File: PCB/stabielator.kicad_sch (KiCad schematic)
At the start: 28 parts, among them SW2 BOOT, U3 ESP32-C3-MINI-1

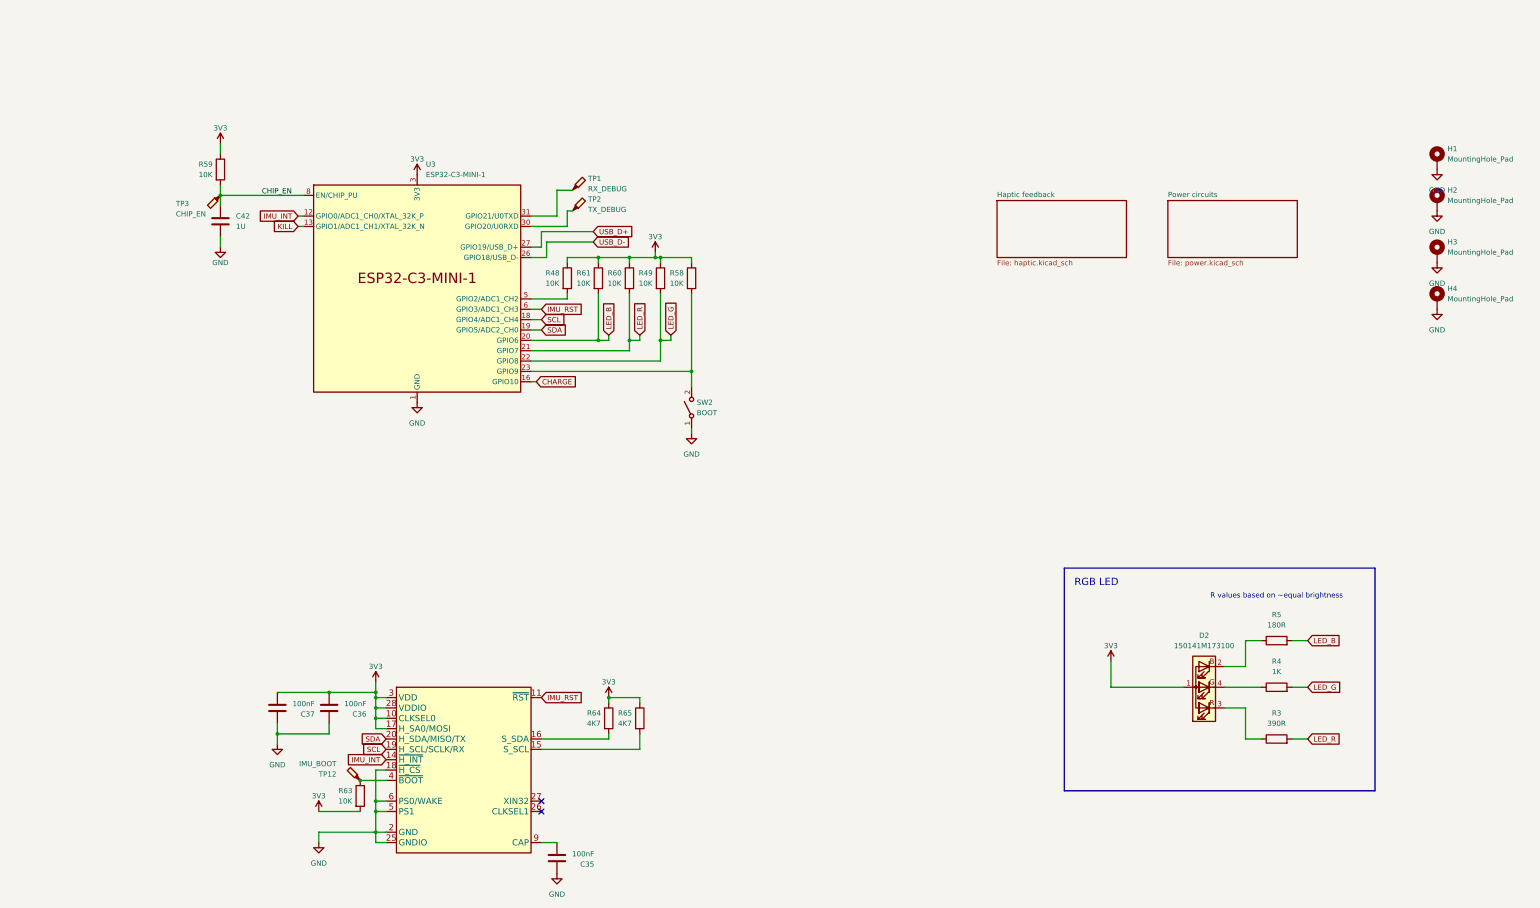
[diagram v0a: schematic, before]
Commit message: Review schematic
Fix errors / add improvements
Add gitignore file
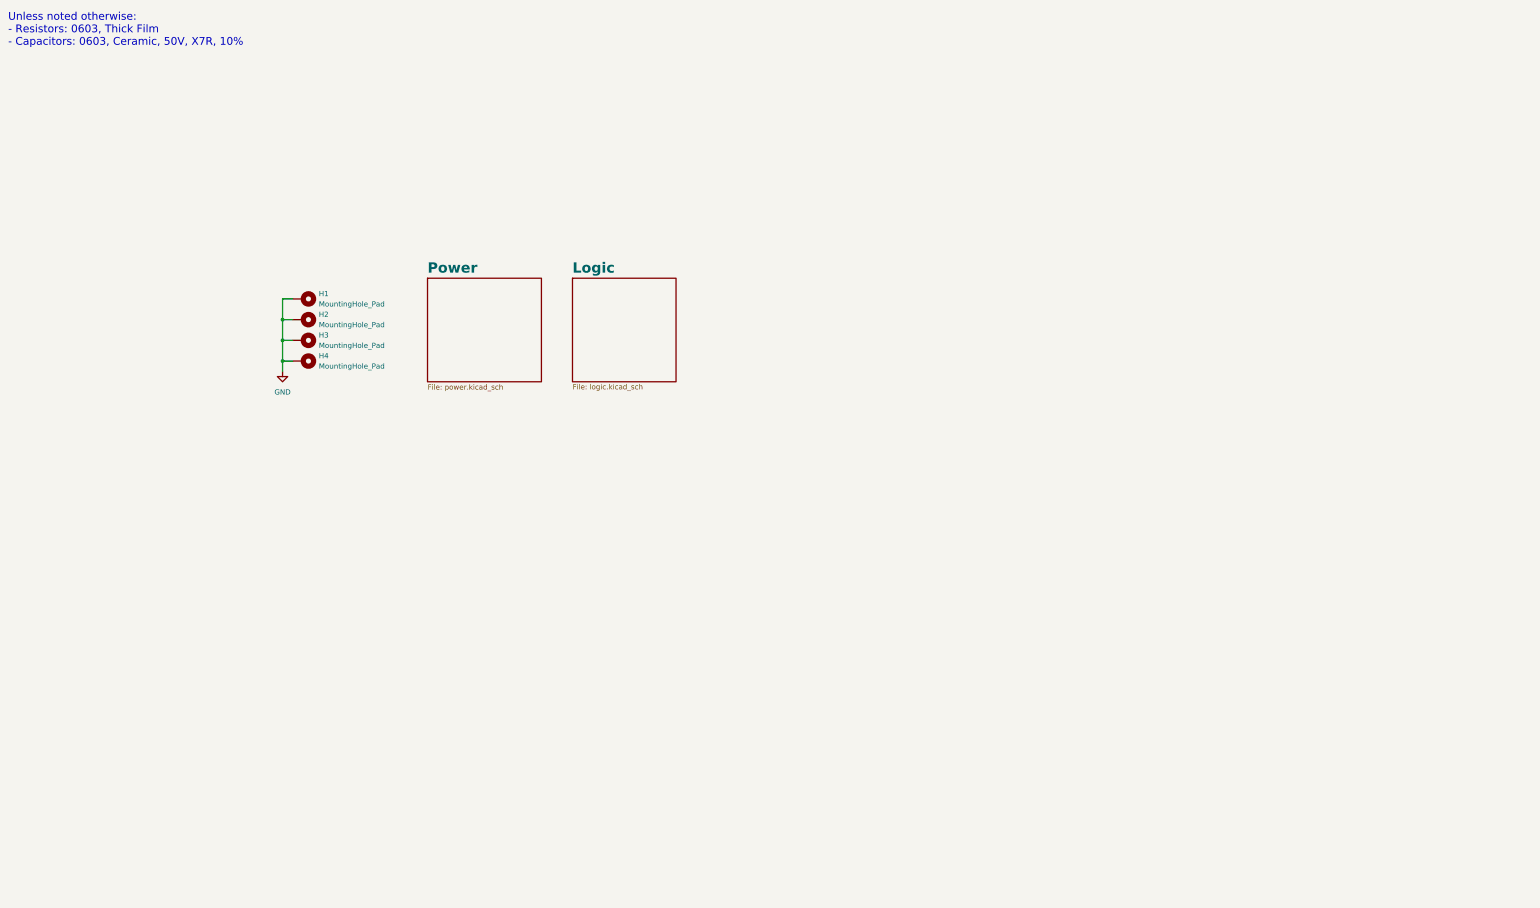
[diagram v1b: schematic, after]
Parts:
- removed C35, C36, C37: 100nF, Capacitor_SMD:C_0603_1608Metric, symbol Device:C
- removed C42: 1U, Capacitor_SMD:C_0603_1608Metric, symbol Device:C
- removed D2: 150141M173100, LED_SMD:LED_RGB_Wuerth-PLCC4_3.2x2.8mm_150141M173100, symbol Device:LED_ABRG
- removed R3: 390R, Resistor_SMD:R_0603_1608Metric, symbol Device:R
- removed R4: 1K, Resistor_SMD:R_0603_1608Metric, symbol Device:R
- removed R48, R49, R58, R59, R60, R61, R63: 10K, Resistor_SMD:R_0603_1608Metric, symbol Device:R
- removed R5: 180R, Resistor_SMD:R_0603_1608Metric, symbol Device:R
- removed R64, R65: 4K7, Resistor_SMD:R_0603_1608Metric, symbol Device:R
- removed SW2: BOOT, Button_Switch_SMD:SW_SPST_B3U-1000P, symbol Switch:SW_SPST
- removed TP1: RX_DEBUG, TestPoint:TestPoint_Pad_D1.0mm, symbol Connector:TestPoint_Probe
- removed TP12: IMU_BOOT, TestPoint:TestPoint_Pad_D1.0mm, symbol Connector:TestPoint_Probe
- removed TP2: TX_DEBUG, TestPoint:TestPoint_Pad_D1.0mm, symbol Connector:TestPoint_Probe
- removed TP3: CHIP_EN, TestPoint:TestPoint_Pad_D1.0mm, symbol Connector:TestPoint_Probe
- removed U2: (no value), stabielator:LGA-28, symbol stabielator:BNO086
- removed U3: ESP32-C3-MINI-1, PCM_Espressif:ESP32-C3-MINI-1, symbol PCM_Espressif:ESP32-C3-MINI-1
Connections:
- no-connect marks 2 -> 0
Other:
- sheet Haptic feedback renamed Logic
- sheet Power circuits renamed Power
- sheet Logic: file haptic.kicad_sch -> logic.kicad_sch
- note added: "Unless noted otherwise: - Resistors: 0603, Thick Film - Capacitors: 0603, Ceramic, 50V, X7R, 10%"
- note removed: "R values based on ~equal brightness"
- note removed: "RGB LED"
- company: ProtoIoT -> ${Company_name}
- title: Stabielator -> ${Project_name}

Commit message: Hopelijk definitief schema
Voornamelijk voeding opnieuw gemaakt;
Vervangen voor een buck boost systeem.
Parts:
- H1, H2, H3, H4: Digikey (none) -> nvt
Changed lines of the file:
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@@
+			)
+		)
+		(property "Digikey" "nvt"
+			(at 88.9 99.06 90)
+			(hide yes)
+			(show_name no)
+			(do_not_autoplace no)
+			(effects
+				(font
+					(size 1.27 1.27)
+				)
 			)
 		)
@@
 			)
 		)
+		(property "Digikey" "nvt"
+			(at 88.9 104.14 90)
+			(hide yes)
+			(show_name no)
+			(do_not_autoplace no)
+			(effects
+				(font
+					(size 1.27 1.27)
+				)
+			)
+		)
 		(pin "1"
 		)
@@
 			)
 		)
+		(property "Digikey" "nvt"
+			(at 88.9 88.9 90)
+			(hide yes)
+			(show_name no)
+			(do_not_autoplace no)
+			(effects
+				(font
+					(size 1.27 1.27)
+				)
+			)
+		)
 		(pin "1"
 		)
@@
 			(hide yes)
 			(show_name no)
+			(do_not_autoplace no)
+			(effects
+				(font
+					(size 1.27 1.27)
+				)
+			)
+		)
+		(property "Digikey" "nvt"
+			(at 88.9 93.98 90)
+			(hide yes)
+			(show_name no)

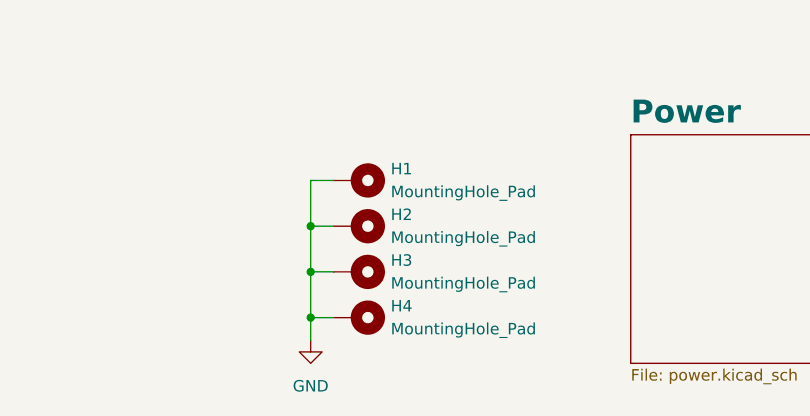
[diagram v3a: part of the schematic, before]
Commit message: Reannotated schematic based on component placement
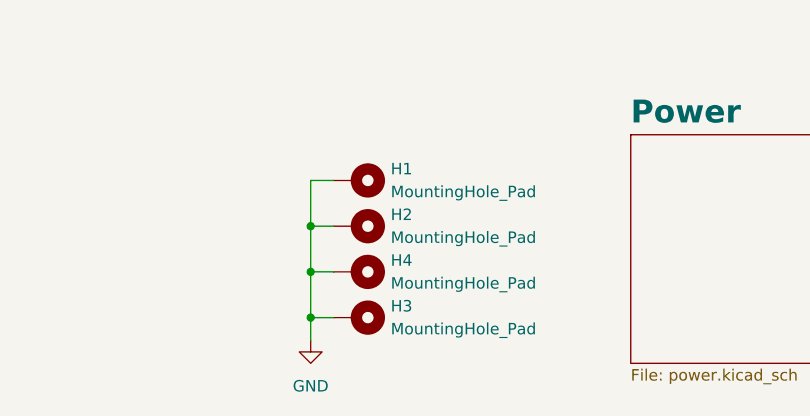
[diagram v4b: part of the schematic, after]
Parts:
- renumbered H4 to H3, H3 to H4
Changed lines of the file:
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@@
 		(dnp no)
 		(fields_autoplaced yes)
-		(property "Reference" "H3"
+		(property "Reference" "H4"
 			(at 92.71 97.7899 90)
 			(show_name no)
@@
 			(project "stabielator"
 				(path "/c0e871b7-8ed4-4f9b-ae4f-e503a34d56f3"
-					(reference "H3")
+					(reference "H4")
 					(unit 1)
 				)
@@
 		(dnp no)
 		(fields_autoplaced yes)
-		(property "Reference" "H4"
+		(property "Reference" "H3"
 			(at 92.71 102.8699 90)
 			(show_name no)
@@
 			(project "stabielator"
 				(path "/c0e871b7-8ed4-4f9b-ae4f-e503a34d56f3"
-					(reference "H4")
+					(reference "H3")
 					(unit 1)
 				)

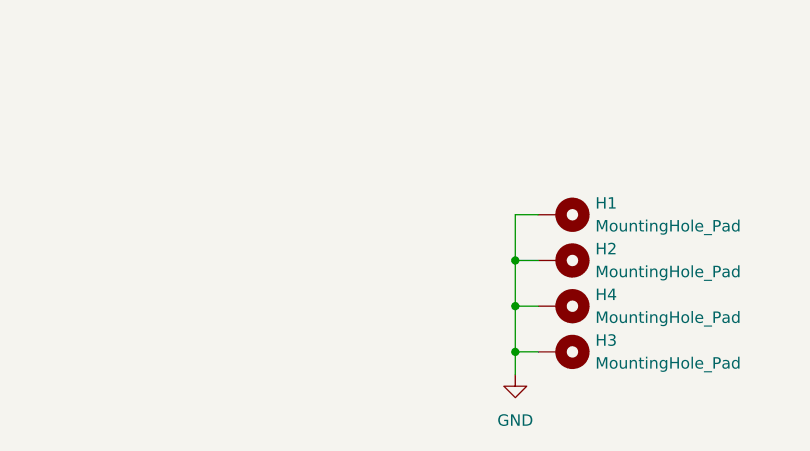
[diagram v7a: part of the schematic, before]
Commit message: Feedback Elect
- Thermal reliefs toegepast op een aantal extra onderdelen
- U7 (LGA-28) footprint pads + pasta/masker aangepast (80% pasta dekking aangeraden door fabrikant)
- Algemene soldeer masker expansie op 0 gezet
- 2x 0.5mm fiducial toegevoegd
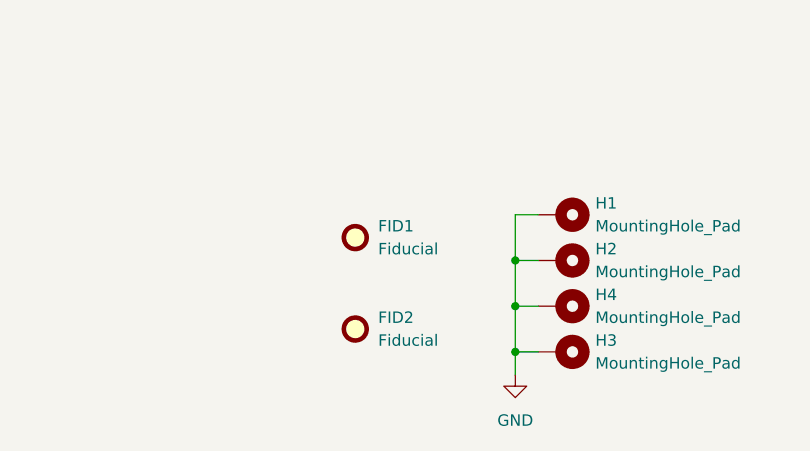
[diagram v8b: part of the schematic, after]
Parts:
- added FID1, FID2: Fiducial, Fiducial:Fiducial_0.5mm_Mask1mm, symbol symbols:Fiducial
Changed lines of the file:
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@@
+	)
+	(symbol
+		(lib_id "symbols:Fiducial")
+		(at 66.04 101.6 0)
+		(unit 1)
+		(body_style 1)
+		(exclude_from_sim no)
+		(in_bom no)
+		(on_board yes)
+		(in_pos_files yes)
+		(dnp no)
+		(fields_autoplaced yes)
+		(property "Reference" "FID2"
+			(at 68.58 100.3299 0)
+			(show_name no)
+			(do_not_autoplace no)
+			(effects
+				(font
+					(size 1.27 1.27)
+				)
+				(justify left)
+			)
+		)
+		(property "Value" "Fiducial"
+			(at 68.58 102.8699 0)
+			(show_name no)
+			(do_not_autoplace no)
+			(effects
+				(font
+					(size 1.27 1.27)
+				)
+				(justify left)
+			)
+		)
+		(property "Footprint" "Fiducial:Fiducial_0.5mm_Mask1mm"
+			(at 66.04 101.6 0)
+			(hide yes)
+			(show_name no)
+			(do_not_autoplace no)
+			(effects
+				(font
+					(size 1.27 1.27)
+				)
+			)
+		)
+		(property "Datasheet" ""
+			(at 66.04 101.6 0)
+			(hide yes)
+			(show_name no)
+			(do_not_autoplace no)
+			(effects
+				(font
+					(size 1.27 1.27)
+				)
+			)
+		)
+		(property "Description" "Fiducial Marker"
+			(at 66.04 101.6 0)
+			(hide yes)
+			(show_name no)
+			(do_not_autoplace no)
+			(effects
+				(font
+					(size 1.27 1.27)
+				)
+			)
+		)
+		(instances
+			(project "stabielator"
+				(path "/c0e871b7-8ed4-4f9b-ae4f-e503a34d56f3"
+					(reference "FID2")
+					(unit 1)
+				)
+			)
+		)
+	)
+	(symbol
+		(lib_id "symbols:Fiducial")
+		(at 66.04 91.44 0)
+		(unit 1)
+		(body_style 1)
+		(exclude_from_sim no)
+		(in_bom no)
+		(on_board yes)
+		(in_pos_files yes)
+		(dnp no)
+		(fields_autoplaced yes)
+		(property "Reference" "FID1"
+			(at 68.58 90.1699 0)
+			(show_name no)
+			(do_not_autoplace no)
+			(effects
+				(font
+					(size 1.27 1.27)
+				)
+				(justify left)
+			)
+		)
+		(property "Value" "Fiducial"
+			(at 68.58 92.7099 0)
+			(show_name no)
+			(do_not_autoplace no)
+			(effects
+				(font
+					(size 1.27 1.27)
+				)
+				(justify left)
+			)
+		)
+		(property "Footprint" "Fiducial:Fiducial_0.5mm_Mask1mm"
+			(at 66.04 91.44 0)
+			(hide yes)
+			(show_name no)
+			(do_not_autoplace no)
+			(effects
+				(font
+					(size 1.27 1.27)
+				)
+			)
+		)
+		(property "Datasheet" ""
+			(at 66.04 91.44 0)
+			(hide yes)
+			(show_name no)
+			(do_not_autoplace no)
+			(effects
+				(font
+					(size 1.27 1.27)
+				)
+			)
+		)
+		(property "Description" "Fiducial Marker"
+			(at 66.04 91.44 0)
+			(hide yes)
+			(show_name no)
+			(do_not_autoplace no)
+			(effects
+				(font
+					(size 1.27 1.27)
+				)
+			)
+		)
+		(instances
+			(project "stabielator"
+				(path "/c0e871b7-8ed4-4f9b-ae4f-e503a34d56f3"
+					(reference "FID1")
+					(unit 1)
+				)
+			)
+		)
 	)
 	(symbol
